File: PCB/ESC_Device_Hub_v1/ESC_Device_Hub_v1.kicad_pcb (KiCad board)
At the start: 4 copper layers, 50 x 90 mm, 137 parts, among them J1 Conn_01x04, J10 Conn_01x06, J11 Conn_01x02, J12 Conn_01x02, J13 Conn_01x02, J14 Conn_01x02, J15 Conn_01x02, J16 Conn_01x02, J17 Conn_01x02, J18 Conn_01x02, J19 Conn_01x05, J2 Conn_01x04, J20 Conn_01x01, J21 Conn_01x01, J22 Conn_01x02, J3 Conn_01x04, J4 Conn_01x04, J5 Conn_01x04, J6 Conn_01x04, J7 Conn_01x06, J8 Conn_01x06, J9 Conn_01x06, SW1 SW_Push, SW2 SW_Push, SW3 SW_Coded_SH-7050, U1 ISO1042BQDWVQ1, U10 LM66100DCK, U11 LM66100DCK, U18 USB_Type-C, U2 MCP2562FD-H/MF, U3 IS25LP064D-JLLE, U4 STM32H563RGVx, U6 TLP293, U7 NJM2884U1-33, U8 RFM-0505S, Y1 FC2012SN 32.768K-70NNA0KC0, Y2 XRCGB25M000FFS1AR0

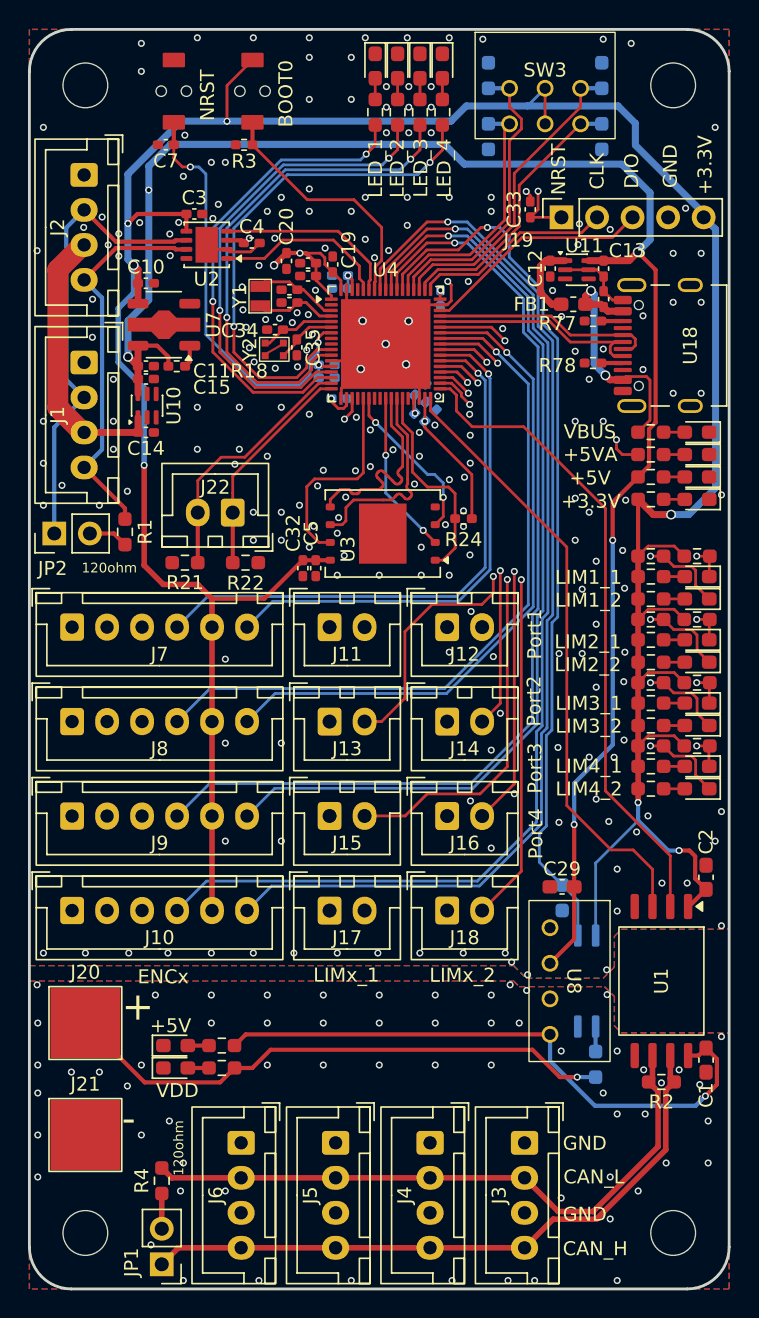
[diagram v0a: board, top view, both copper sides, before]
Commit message: PCBの変更 ID変更 NRSTのパスコン一つ減らした
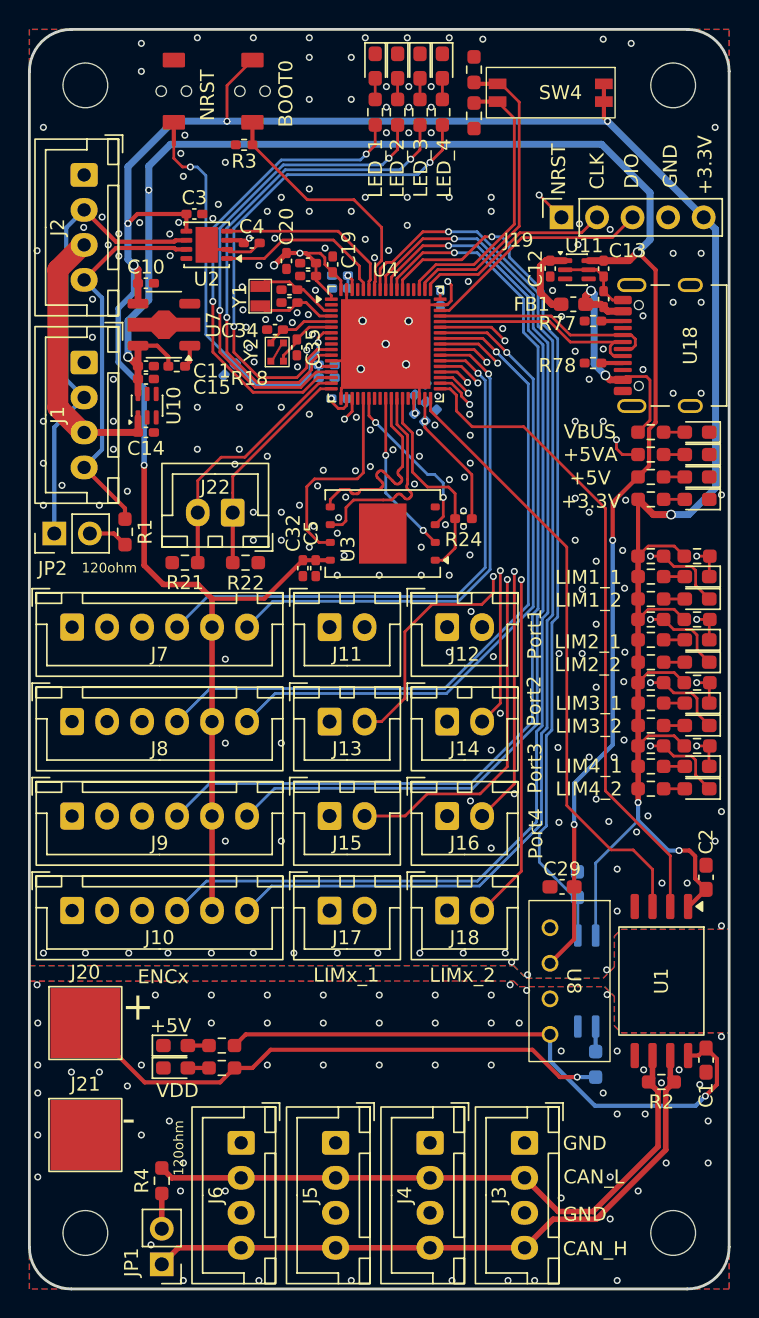
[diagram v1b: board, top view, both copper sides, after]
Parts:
- removed C33: 0.1uF, Capacitor_SMD:C_0402_1005Metric_Pad0.74x0.62mm_HandSolder
- removed R5, R6, R7: 1k, Resistor_SMD:R_0603_1608Metric_Pad0.98x0.95mm_HandSolder
- removed SW3: SW_Coded_SH-7050, My_Library:ERD116RFZ
- added R25: 1k, Resistor_SMD:R_0603_1608Metric_Pad0.98x0.95mm_HandSolder, F.Cu at (171.8, 36.2)
- added SW4: SW_DIP_x02, My_Library:KHS22E, F.Cu at (177.4, 34.5)
- C7: moved to B.Cu
- R20: moved to F.Cu
- moved C7 16.7 mm to (154.3, 54.3), turned to -135 degrees
- moved R20 4.89 mm to (171.8, 32.9)
- moved R19 1.44 mm to (179.2, 91.1), turned to 90 degrees
- moved Y2 0.28 mm to (157.7, 53.1), turned to 90 degrees
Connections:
- R20 pad 1: GND -> ID_4
- R20 pad 2: Rol_SW8 -> GND
- U4 pad 53: Rol_SW2 -> ID_4
- U4 pad 54: Rol_SW1 -> ID_2
- U4 pad 55: Rol_SW4 -> unconnected-(U4-PC11-Pad55)
- U4 pad 56: Rol_SW8 -> unconnected-(U4-PC12-Pad56)
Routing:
- net Rol_SW1: track 22.4 -> 0.00 mm
- net ID_4: track 0.00 -> 21.6 mm
- net Rol_SW4: track 21.2 -> 0.00 mm
- net ID_2: track 0.00 -> 20.1 mm
- net Rol_SW2: track 19.6 -> 0.00 mm
- net Rol_SW8: track 18.1 -> 0.00 mm
- net +3.3V: track 285.5 -> 282.3 mm, vias 13 -> 14
- net NRST: track 59.9 -> 57.9 mm
- net POWER_MONITOR: track 63.4 -> 62.3 mm
- net GND: track 37.9 -> 37.1 mm, vias 217 -> 214
- net ENC3_A: track 68.5 -> 67.7 mm
- net ENC4_B: track 81.8 -> 81.0 mm
- net ENC3_B: track 71.8 -> 71.0 mm
- net HSE_OUT: track 4.19 -> 4.77 mm
- net ENC4_A: track 78.6 -> 78.0 mm

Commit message: ビア追加
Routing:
- net GND: vias 214 -> 225

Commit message: 原因不明
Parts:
- removed J19: Conn_01x05, Connector_PinSocket_2.54mm:PinSocket_1x05_P2.54mm_Vertical
- added J23: Conn_01x04, Connector_PinSocket_2.54mm:PinSocket_1x04_P2.54mm_Vertical, F.Cu at (180.6, 43.4)
- C7: moved to F.Cu
- moved C7 16.8 mm to (149.8, 38.2), turned to 180 degrees
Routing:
- net NRST: track 57.9 -> 29.9 mm, vias 3 -> 2
- net GND: vias 225 -> 228
